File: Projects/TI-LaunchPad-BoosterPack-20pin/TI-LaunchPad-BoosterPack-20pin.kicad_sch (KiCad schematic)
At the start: 2 parts, among them J1 Conn_01x10, J2 Conn_01x10

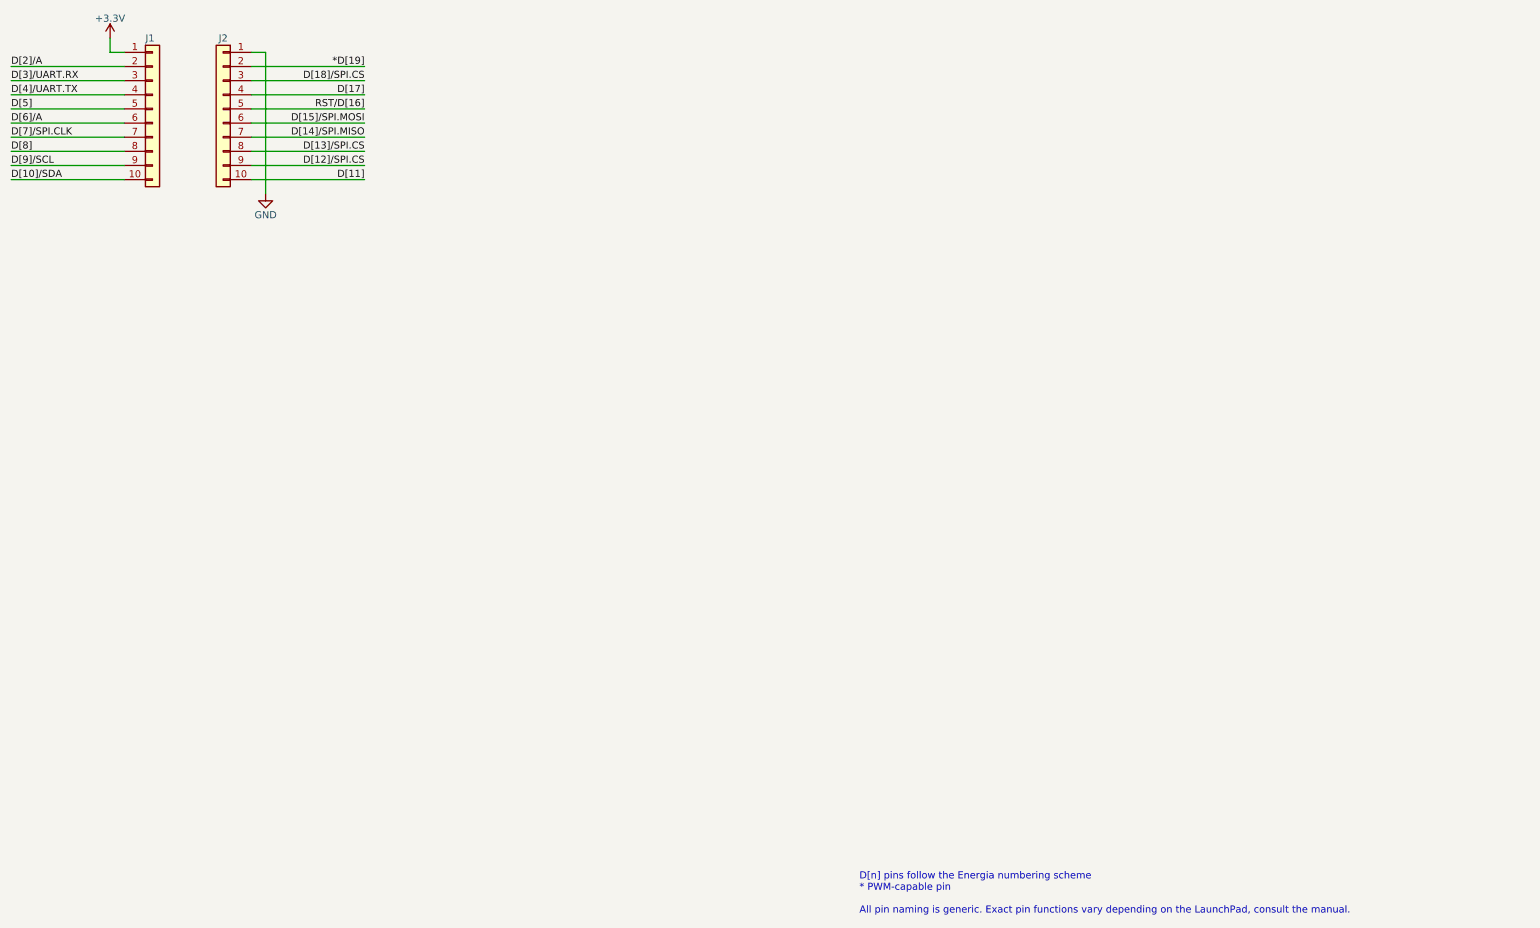
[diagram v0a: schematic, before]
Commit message: Update projects for KiCad version 7
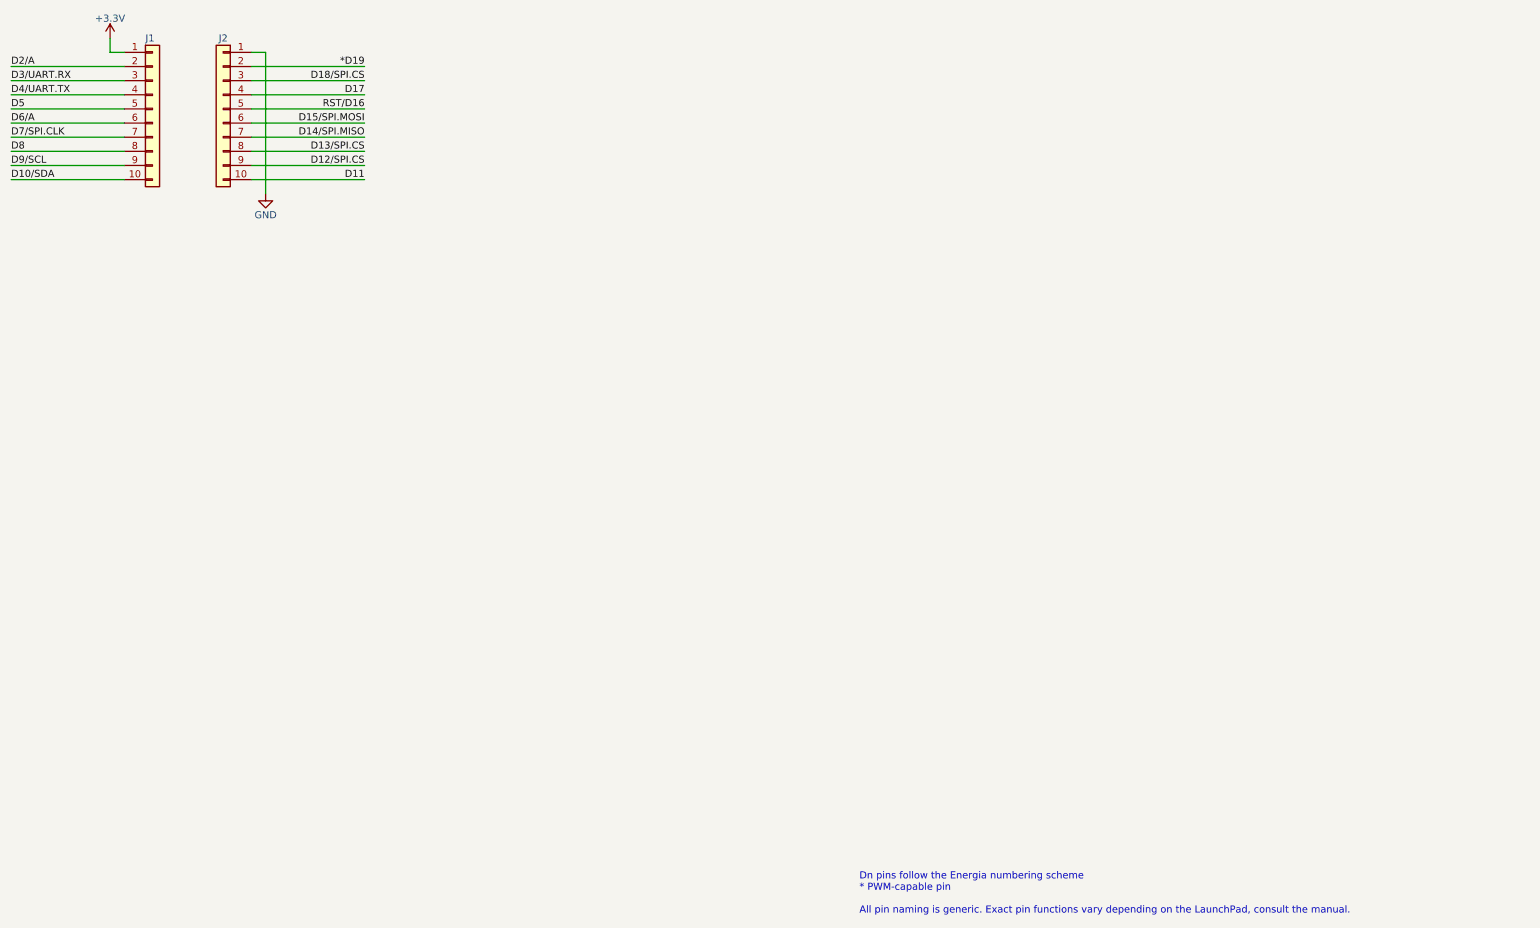
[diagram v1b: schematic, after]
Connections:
- net *D[19] renamed *D19
- net D[10]/SDA renamed D10/SDA
- net D[11] renamed D11
- net D[12]/SPI.CS renamed D12/SPI.CS
- net D[13]/SPI.CS renamed D13/SPI.CS
- net D[14]/SPI.MISO renamed D14/SPI.MISO
- net D[15]/SPI.MOSI renamed D15/SPI.MOSI
- net D[17] renamed D17
- net D[18]/SPI.CS renamed D18/SPI.CS
- net D[2]/A renamed D2/A
- net D[3]/UART.RX renamed D3/UART.RX
- net D[4]/UART.TX renamed D4/UART.TX
- net D[5] renamed D5
- net D[6]/A renamed D6/A
- net D[7]/SPI.CLK renamed D7/SPI.CLK
- net D[8] renamed D8
- net D[9]/SCL renamed D9/SCL
- net RST/D[16] renamed RST/D16
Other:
- note added: "Dn pins follow the Energia numbering scheme * PWM-capable pin All pin naming is generic. Exact pin functions vary depending on the LaunchPad, consult the manual."
- note removed: "D[n] pins follow the Energia numbering scheme * PWM-capable pin All pin naming is generic. Exact pin functions vary depending on the LaunchPad, consult the manual."

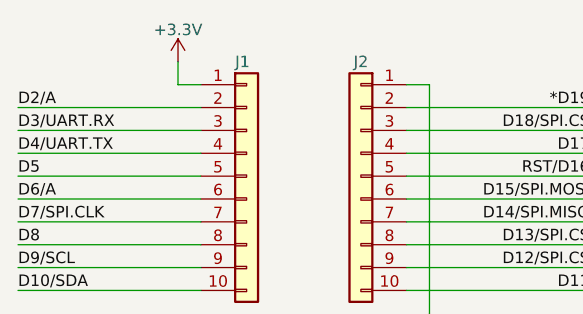
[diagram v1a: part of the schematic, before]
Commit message: Update templates to V8 format
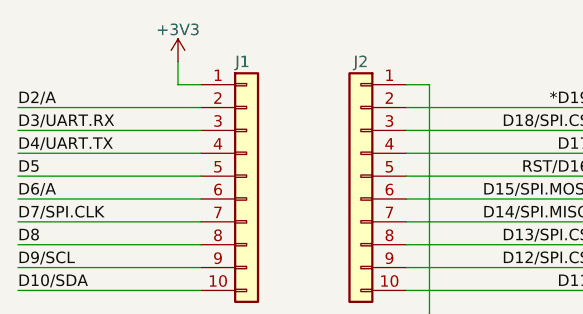
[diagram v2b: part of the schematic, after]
